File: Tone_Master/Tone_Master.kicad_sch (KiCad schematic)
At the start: 49 parts, among them J1 Barrel_Jack, J2 Barrel_Jack, Q1 2N3904, Q2 2N3904, SW2 DSP_EN, SW3 Chorus_EN, SW4 SW_Rotary_4x3, U1 TL072, U2 TL072

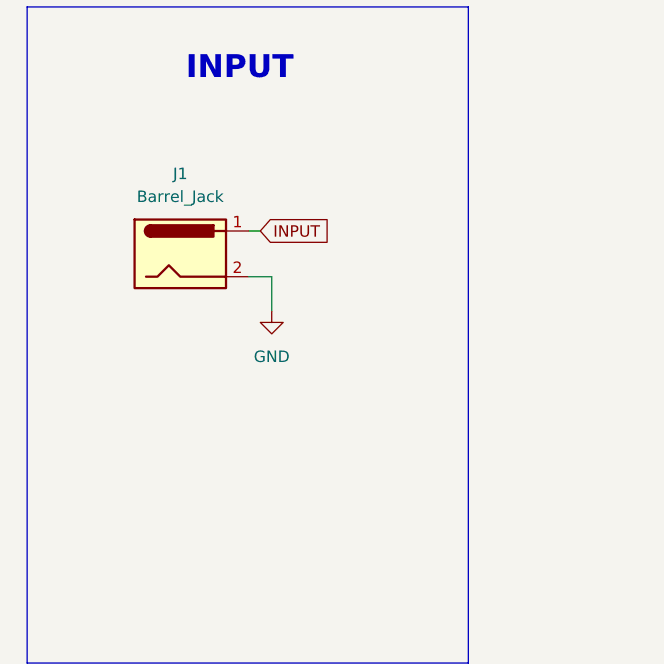
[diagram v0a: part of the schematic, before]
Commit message: add block diagram
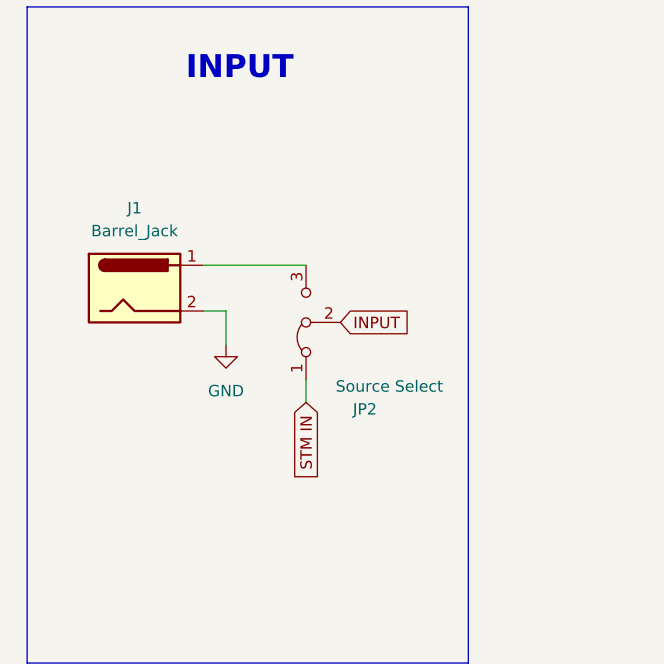
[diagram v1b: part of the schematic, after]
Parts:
- added JP2: Source Select, symbol Jumper:Jumper_3_Bridged12
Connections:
- net INPUT: now also JP2.2 (C); no longer J1.1
- new net: J1.1, JP2.3 (B)
- new net STM IN: JP2.1 (A)

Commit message: add BOM
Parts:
- removed C3: 50pF, Capacitor_THT:C_Rect_L7.2mm_W3.0mm_P5.00mm_FKS2_FKP2_MKS2_MKP2, symbol Device:C
- removed SW4: SW_Rotary_4x3, symbol Switch:SW_Rotary_4x3
- added C7: 50pF, Capacitor_THT:C_Rect_L7.2mm_W3.0mm_P5.00mm_FKS2_FKP2_MKS2_MKP2, symbol Device:C
- added R5, R6: 10K, Resistor_SMD:R_0805_2012Metric_Pad1.20x1.40mm_HandSolder, symbol Device:R
- added SW1: SW_Rotary_3x4, symbol Switch:SW_Rotary_3x4
- C5: renamed from C1; value 470nF -> 22nF
- renumbered C4 to C1, C13 to C10, C17 to C12, C15 to C13, C6 to C14, C12 to C15, C7 to C16, C5 to C17, C9 to C2, C2 to C3, C10 to C4, C18 to C6, C16 to C8, C8 to C9, D2 to D1, D1 to D2, J2 to J1, J1 to J2, JP2 to JP1, JP1 to JP2, Q2 to Q1, Q1 to Q2, R2 to R1, R13 to R10, R9 to R11, R7 to R12, R5 to R13, R8 to R14, R4 to R15, R14 to R16, R6 to R2, R1 to R4, R11 to R7, R12 to R8, R10 to R9, RV4 to RV2, RV2 to RV3, U2 to U1, U1 to U2
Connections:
- net DISTORT_IN: now also R6.2; no longer C5.1
- net DISTORT_OUT: now also SW1.10
- net FUZZ_OUT: now also SW1.11
- net GND: now also C7.2, SW1.7
- net OD_IN: now also R5.1; no longer C3.1
- net OD_OUT: now also SW1.9
- net Signal_OUT: now also SW1.15
- net at C4.1, D1.2 (A), D3.1 (K)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: now also SW1.1
- net at C9.2, RV1.2: now also SW1.13
- net at RV1.3: now also SW1.14
- net at U2.1: now also SW1.2
- net at C12.1: now also SW1.3
- net at C11.2: now also SW1.6
- net PICKUP_OUT: now reaches J2.1, JP1.3 (B)
- net STM IN renamed STM OUT
- new net: C3.1, R5.2
- new net: C5.1, C7.1, R6.1
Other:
- moved on the sheet: C5, R4, U1B

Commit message: Todo: input buffer
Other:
- note added: "PICKUP TO STM"
- moved on the sheet: U1B
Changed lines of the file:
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@@
 	(wire
 		(pts
-			(xy 45.72 210.82) (xy 59.69 210.82)
+			(xy 46.99 210.82) (xy 59.69 210.82)
 		)
 		(stroke
@@
 	)
 	(rectangle
-		(start 28.702 160.528)
-		(end 77.724 233.426)
+		(start 28.448 218.948)
+		(end 77.47 262.382)
+		(stroke
+			(width 0)
+			(type default)
+		)
+		(fill
+			(type none)
+		)
+	)
+	(rectangle
+		(start 28.702 173.228)
+		(end 77.724 216.916)
 		(stroke
 			(width 0)
@@
 	(text "INPUT"
 		(exclude_from_sim no)
-		(at 52.324 167.386 0)
+		(at 52.324 179.832 0)
 		(effects
 			(font
@@
 		(exclude_from_sim no)
 		(at 329.184 33.528 0)
+		(effects
+			(font
+				(size 2.54 2.54)
+				(thickness 0.254)
+				(bold yes)
+			)
+		)
+	)
+	(text "PICKUP TO STM"
+		(exclude_from_sim no)
+		(at 52.07 223.52 0)
 		(effects
 			(font
@@
 		)
 	)
-	(global_label "STM OUT"
+	(global_label "PICKUP_OUT"
 		(shape input)
-		(at 45.72 210.82 180)
+		(at 44.45 242.57 180)
 		(fields_autoplaced yes)
 		(effects
@@
 		)
 		(property "Intersheetrefs" "${INTERSHEET_REFS}"
-			(at 34.5101 210.82 0)
+			(at 29.8533 242.57 0)
 			(effects
 				(font
@@
 				)
 				(justify left)
+				(hide yes)
+			)
+		)
+	)
+	(global_label "STM OUT"
+		(shape input)
+		(at 46.99 210.82 180)
+		(fields_autoplaced yes)
+		(effects
+			(font
+				(size 1.27 1.27)
+			)
+			(justify right)
+		)
+		(property "Intersheetrefs" "${INTERSHEET_REFS}"
+			(at 35.7801 210.82 0)
+			(effects
+				(font
+					(size 1.27 1.27)
+				)
+				(justify right)
 				(hide yes)
 			)
@@
 	(symbol
 		(lib_id "Amplifier_Operational:TL072")
-		(at 441.96 187.96 0)
+		(at 57.15 245.11 0)
 		(unit 2)
 		(exclude_from_sim no)
@@
 		(dnp no)
 		(property "Reference" "U1"
-			(at 441.96 177.8 0)
+			(at 57.15 234.95 0)
 			(effects
 				(font
@@
 		)
 		(property "Value" "TL072"
-			(at 441.96 180.34 0)
+			(at 57.15 237.49 0)
 			(effects
 				(font
@@
 		)
 		(property "Footprint" "Package_DIP:DIP-8_W7.62mm"
-			(at 441.96 187.96 0)
+			(at 57.15 245.11 0)
 			(effects
 				(font
@@
 		)
 		(property "Datasheet" "http://www.ti.com/lit/ds/symlink/tl071.pdf"
-			(at 441.96 187.96 0)
+			(at 57.15 245.11 0)
 			(effects
 				(font
@@
 		)
 		(property "Description" "Dual Low-Noise JFET-Input Operational Amplifiers, DIP-8/SOIC-8"
-			(at 441.96 187.96 0)
-			(effects
-				(font
+			(at 57.15 245.11 0)
+			(effects
+				(font

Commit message: full schematic v1
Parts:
- removed J1: Barrel_Jack, Connector_BarrelJack:BarrelJack_SwitchcraftConxall_RAPC10U_Horizontal, symbol Connector:Barrel_Jack
- added C18, C19: 1uF, Capacitor_THT:CP_Radial_D8.0mm_P5.00mm, symbol Device:C_Polarized_Small_US
- added C20: 470nF, Capacitor_THT:C_Rect_L7.2mm_W3.0mm_P5.00mm_FKS2_FKP2_MKS2_MKP2, symbol Device:C
- added C21: 47uF, Capacitor_THT:CP_Radial_D8.0mm_P5.00mm, symbol Device:C_Polarized_Small_US
- added C22: 47nF, symbol Device:C
- added Q3: TIP41C, Package_TO_SOT_THT:TO-220-3_Vertical, symbol Transistor_BJT:TIP41C
- added Q4: TIP42C, Package_TO_SOT_THT:TO-220-3_Vertical, symbol Transistor_BJT:TIP42C
- added R19, R24: 1Meg, symbol Device:R
- added R22: 47k, symbol Device:R
- added R23: 3K, symbol Device:R
- added R25: 10k, symbol Device:R
- added R26: 22k, symbol Device:R
- added U3: TL072, Package_DIP:DIP-8_W7.62mm, symbol Amplifier_Operational:TL072
- added U4: ~, Black Pill:STM32 Black Pill, symbol STM32_Black_Pill:SW_DIP_x10
- added U5: LM7805_TO220, Package_TO_SOT_THT:TO-220-3_Horizontal_TabDown, symbol Regulator_Linear:LM7805_TO220
- added U6, U7: MCP4725xxx-xCH, Package_TO_SOT_SMD:SOT-23-6, symbol Analog_DAC:MCP4725xxx-xCH
- added U8: LP2950-3.3_TO92, Package_TO_SOT_THT:TO-92_Inline, symbol Regulator_Linear:LP2950-3.3_TO92
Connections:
- net +9V: now also Q3.2 (C), R22.1, U3.8 (V+), U5.1 (VI)
- net 4.5V_ref: now also C18.1, R19.1
- net GND: now also C21.2, C22.2, Q4.2 (C), R23.2, U3.4 (V-), U4.47 (GND), U5.2 (GND), U6.2 (VSS), U7.6 (GND), U8.2 (GND)
- net PICKUP_OUT: now also C20.1, U4.10 (A0)
- net STM OUT: now also U6.1 (VOUT)
- net at U1.5 (+): now also C20.2, R24.1
- net at U1.6 (-): now also R25.1, R26.1
- net Preamp_OUT: now reaches U1.7
- net Preamp_OUT: now also R26.2
- net OUTPUT: no longer names the net of RV3.2
- net OUTPUT: now also C18.2
- new net: C21.1, R22.2, R23.1, R24.2
- new net: C22.1, R25.2
- new net: Q3.1 (B), Q4.1 (B), U3.1
- new net: C19.1, Q3.3 (E), Q4.3 (E), U3.2 (-)
- new net: R19.2, U3.3 (+)
- new net: U7.5 (VDD), U8.1 (VO)
- new net 5V: U4.5V, U5.3 (VO), U6.3 (VDD), U8.3 (VI)
- new net AUDIO_OUT: C19.2
- new net SCK: U4.13 (A3), U7.3 (WS)
- new net SCL: U4.42 (B6), U6.5 (SCL)
- new net SD: U7.4 (SD)
- new net SDA: U4.43 (B7), U6.4 (SDA)
- new net WS: U4.12 (23), U7.3 (WS)
- no-connect marks 0 -> 30
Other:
- note added: "Black Pill"
- note added: "DAC"
- note added: "I^{2}S MIC MODULE"
- note added: "POWER AMPLIFIER"
- note removed: "OUTPUT"
- moved on the sheet: C1, C10, C11, C12, C13, C14, C15, C16, C17, C2, C3, C4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

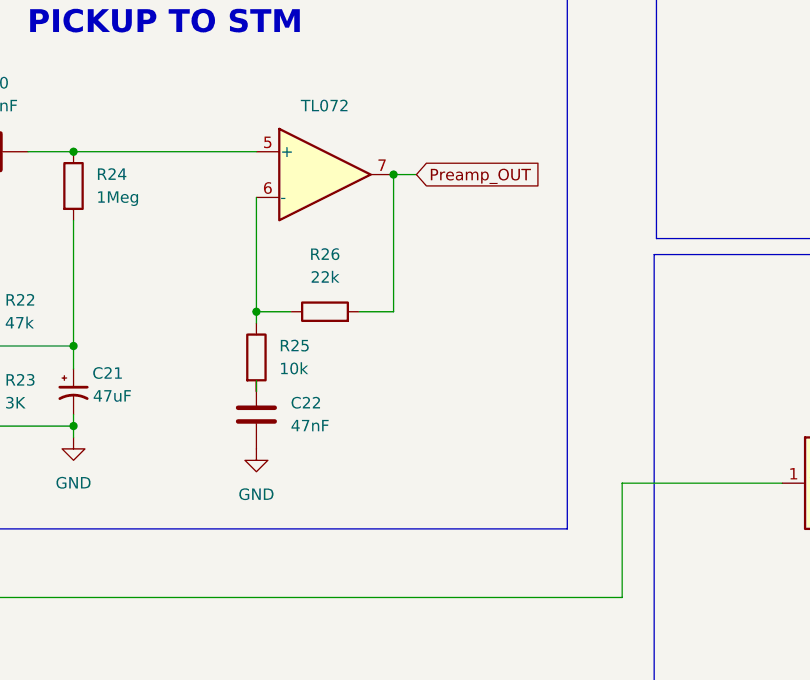
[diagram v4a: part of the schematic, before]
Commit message: Add voltage protection
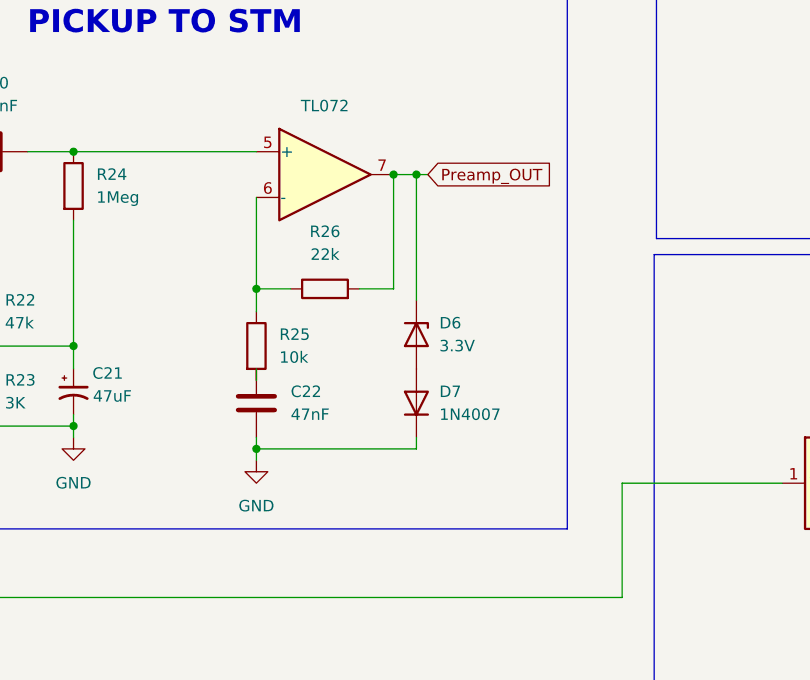
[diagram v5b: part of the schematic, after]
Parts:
- added D6: 3.3V, Diode_THT:D_DO-41_SOD81_P7.62mm_Horizontal, symbol Device:D_Zener
- added D7: 1N4007, Diode_THT:D_DO-41_SOD81_P7.62mm_Horizontal, symbol Device:D
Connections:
- net GND: now also D7.1 (K)
- net Preamp_OUT: now also D6.1 (K)
- new net: D6.2 (A), D7.2 (A)
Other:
- moved on the sheet: C22, R25, R26

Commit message: R2
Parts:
- removed D3: 1N4148, Diode_THT:D_DO-35_SOD27_P7.62mm_Horizontal, symbol Diode:1N4148
- removed JP2: Tone Control Select, symbol Jumper:Jumper_3_Bridged12
- removed Q3: TIP41C, Package_TO_SOT_THT:TO-220-3_Vertical, symbol Transistor_BJT:TIP41C
- removed Q4: TIP42C, Package_TO_SOT_THT:TO-220-3_Vertical, symbol Transistor_BJT:TIP42C
- removed R19: 1Meg, symbol Device:R
- removed unit 2 of U3
- removed unit 1 of U3
- removed U8: LP2950-3.3_TO92, Package_TO_SOT_THT:TO-92_Inline, symbol Regulator_Linear:LP2950-3.3_TO92
- added C23: 330n, Capacitor_THT:CP_Radial_D8.0mm_P5.00mm, symbol Device:C_Polarized_Small_US
- added C24: 10u, Capacitor_THT:C_Rect_L7.2mm_W3.0mm_P5.00mm_FKS2_FKP2_MKS2_MKP2, symbol Device:C
- added C25: 330n, Capacitor_THT:C_Rect_L7.2mm_W3.0mm_P5.00mm_FKS2_FKP2_MKS2_MKP2, symbol Device:C
- added C26: 47p, Capacitor_THT:C_Rect_L7.2mm_W3.0mm_P5.00mm_FKS2_FKP2_MKS2_MKP2, symbol Device:C
- added C27: 180n, Capacitor_THT:CP_Radial_D8.0mm_P5.00mm, symbol Device:C_Polarized_Small_US
- added R17: 10, Resistor_THT:R_Axial_DIN0309_L9.0mm_D3.2mm_P12.70mm_Horizontal, symbol Device:R
- added U8: LM386, symbol Amplifier_Audio:LM386
- C18: value 1uF -> 330n
- C19: value 1uF -> 1000uF
- C22: footprint (none) -> Capacitor_THT:C_Rect_L7.2mm_W3.0mm_P5.00mm_FKS2_FKP2_MKS2_MKP2
- D4: footprint LED_SMD:LED_1206_3216Metric_Pad1.42x1.75mm_HandSolder -> LED_THT:LED_D3.0mm_Clear
- D5: footprint (none) -> LED_THT:LED_D3.0mm_Clear
- JP1: footprint (none) -> Connector_PinHeader_2.54mm:PinHeader_1x02_P2.54mm_Vertical
- R1, R10, R11, R12, R13, R15, R16, R2, R3, R4, R5, R6, R7, R8: footprint Resistor_SMD:R_0805_2012Metric_Pad1.20x1.40mm_HandSolder -> Resistor_THT:R_Axial_DIN0309_L9.0mm_D3.2mm_P12.70mm_Horizontal
- R14: value 330K -> 680K; footprint Resistor_SMD:R_0805_2012Metric_Pad1.20x1.40mm_HandSolder -> Resistor_THT:R_Axial_DIN0309_L9.0mm_D3.2mm_P12.70mm_Horizontal
- R22, R24, R25: footprint (none) -> Resistor_THT:R_Axial_DIN0309_L9.0mm_D3.2mm_P12.70mm_Horizontal
- R23: value 3K -> 10K; footprint (none) -> Resistor_THT:R_Axial_DIN0309_L9.0mm_D3.2mm_P12.70mm_Horizontal
- R26: value 22k -> 33K; footprint (none) -> Resistor_THT:R_Axial_DIN0309_L9.0mm_D3.2mm_P12.70mm_Horizontal
- R9: value 10k -> 33K; footprint Resistor_SMD:R_0805_2012Metric_Pad1.20x1.40mm_HandSolder -> Resistor_THT:R_Axial_DIN0309_L9.0mm_D3.2mm_P12.70mm_Horizontal
- RV1: value 10K -> 100k
- SW2, SW3: footprint (none) -> Button_Switch_THT:SW_SPST_Omron_B3F-40xx
- U2: footprint (none) -> Package_DIP:DIP-8_W7.62mm
- U4: footprint Black Pill:STM32 Black Pill -> Module:Arduino_Nano
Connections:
- net Chorus is gone; now on net SW_Effect: SW3.2
- net DISTORT_OUT is gone; now on net DISTORT_IN: SW1.10
- net +9V: now also C25.1, U8.6 (V+)
- net 4.5V_ref: no longer C18.1
- net DSP: now also U4.15 (A5)
- net FUZZ_IN: now also SW1.11
- net FUZZ_OUT: no longer SW1.11
- net GND: now also C23.2, C24.2, C25.2, C26.1, C27.2, U8.4 (GND)
- net OD_IN: now also SW1.9
- net OD_OUT: no longer SW1.9
- net PICKUP_OUT: no longer U4.10 (A0)
- net Signal_OUT: now also C16.2, R16.2; no longer SW1.15
- net at C4.1, D1.2 (A), SW1.1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: now also D2.1 (K)
- net at C9.1, D1.1 (K), D2.2 (A)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: now also Q1.1 (E); no longer C8.1, Q2.2 (B)
- net SW_Effect: now reaches U4.16 (A6)
- net 3V3: now reaches U4.48 (3V3)
- net 3V3: now also U7.5 (VDD)
- net at C19.1: now also R17.1, U8.5
- net at R10.2: now also C8.1, Q2.2 (B); no longer Q1.1 (E)
- new net: C27.1, R17.2
- new net: C18.1, C26.2, U8.3 (+)
- new net: C23.1, U8.2 (-)
- new net: C24.1, U8.7 (BYPASS)
- new net PREAMP_OUT: U4.10 (A0)
- new net Signal_IN: SW1.15
- no-connect marks 30 -> 32
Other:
- note added: "GUITAR AMP, EFFECTS AND REALTIME TONE SAMPLER"
- moved on the sheet: C14, C19, D2, D6, D7, R10, R13, R24, RV1, U6

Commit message: Final
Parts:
- removed U6: MCP4725xxx-xCH, Package_TO_SOT_SMD:SOT-23-6, symbol Analog_DAC:MCP4725xxx-xCH
- added C28: 10u, Capacitor_THT:CP_Radial_D8.0mm_P5.00mm, symbol Device:C_Polarized_Small_US
- added C29: 330n, Capacitor_THT:CP_Radial_D8.0mm_P5.00mm, symbol Device:C_Polarized_Small_US
- added D3: 1N4148, Diode_THT:D_DO-35_SOD27_P7.62mm_Horizontal, symbol Diode:1N4148
- added R19: 22k, Resistor_THT:R_Axial_DIN0309_L9.0mm_D3.2mm_P12.70mm_Horizontal, symbol Device:R
- added R27, R30: 1Meg, Resistor_THT:R_Axial_DIN0309_L9.0mm_D3.2mm_P12.70mm_Horizontal, symbol Device:R
- added RV4: 10K, Potentiometer_THT:Potentiometer_Piher_PT-15-V02_Vertical, symbol Device:R_Potentiometer
- C13: value 47nF -> 100n
- C14: value 47nF -> 220n
- C18, C23: value 330n -> 270n
- C22: value 47nF -> 100pF
- C25: value 330n -> .33u
- C27: value 180n -> .1u
- C4: value 470nF -> 1uF
- C7: value 50pF -> 100pF
- C8: value 1uF -> 2.2uF
- C9: value 50pF -> 100p
- R10: value 100k -> 120k
- R11: value 680 -> 1k
- R12: value 4.7K -> 10k
- R23: value 10K -> 680
- R26: value 33K -> 120k
- RV3: value 500K -> 470K
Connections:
- net FUZZ_OUT is gone; now on net STM_OUT: C6.2
- net OD_OUT is gone; now on net STM_OUT: C4.2
- net STM OUT is gone; now on an unnamed net: JP1.1 (A)
- net Signal_IN is gone; now on net PICKUP_OUT: SW1.15
- net Signal_OUT is gone; now on net STM_OUT: C16.2, R16.2
- net DISTORT_IN: no longer SW1.10
- net GND: now also R25.2, R27.2, R30.2
- net OD_IN: no longer SW1.9
- net PICKUP_OUT: no longer C20.1
- net Preamp_OUT: now also C20.1, C22.1, R30.1
- net at C4.1, D1.2 (A), U1.1: now also D3.1 (K), R19.2; no longer D2.1 (K), SW1.1
- net Preamp_IN: now reaches SW1.12
- net Preamp_IN: now also SW1.10, SW1.9
- net at U8.1 (GAIN): now also C28.1
- net at U8.8 (GAIN): now also RV4.3
- net Distortion_OUT renamed STM_OUT
- net STM_OUT: now also C29.1, R27.1
- net INPUT: no longer names the net of JP1.2 (C)
- net INPUT: now also C29.2
- net SCL: no longer names the net of U4.42 (B6)
- net SDA: no longer names the net of U4.43 (B7)
- new net: D2.1 (K), D3.2 (A)
- new net: R19.1, SW1.1
- new net: C28.2, RV4.2
- no-connect marks 32 -> 35
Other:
- note added: "PREAMP"
- note added: "Trimpot"
- note removed: "DAC"
- note removed: "PICKUP TO STM"
- moved on the sheet: C19, C20, C27, D2, R17

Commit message: V1.0
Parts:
- removed C22: 100pF, Capacitor_THT:C_Rect_L7.2mm_W3.0mm_P5.00mm_FKS2_FKP2_MKS2_MKP2, symbol Device:C
- removed C29: 330n, Capacitor_THT:CP_Radial_D8.0mm_P5.00mm, symbol Device:C_Polarized_Small_US
- removed D6: 3.3V, Diode_THT:D_DO-41_SOD81_P7.62mm_Horizontal, symbol Device:D_Zener
- removed D7: 1N4007, Diode_THT:D_DO-41_SOD81_P7.62mm_Horizontal, symbol Device:D
- removed JP1: Source Select, Connector_PinHeader_2.54mm:PinHeader_1x02_P2.54mm_Vertical, symbol Jumper:Jumper_3_Bridged12
- removed R30: 1Meg, Resistor_THT:R_Axial_DIN0309_L9.0mm_D3.2mm_P12.70mm_Horizontal, symbol Device:R
- removed SW2: DSP_EN, Button_Switch_THT:SW_SPST_Omron_B3F-40xx, symbol Switch:SW_Push
- removed SW3: Chorus_EN, Button_Switch_THT:SW_SPST_Omron_B3F-40xx, symbol Switch:SW_Push
- removed U4: ~, Module:Arduino_Nano, symbol STM32_Black_Pill:SW_DIP_x10
- removed U5: LM7805_TO220, Package_TO_SOT_THT:TO-220-3_Horizontal_TabDown, symbol Regulator_Linear:LM7805_TO220
- removed U7: MCP4725xxx-xCH, Package_TO_SOT_SMD:SOT-23-6, symbol Analog_DAC:MCP4725xxx-xCH
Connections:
- net DISTORT_IN is gone; now on net Preamp_OUT: R6.2
- net OD_IN is gone; now on net Preamp_OUT: R5.1
- net Preamp_IN: now also C20.1
- net Preamp_OUT: no longer C20.1
- net STM_OUT renamed DISTORT_OUT
- no-connect marks 35 -> 4
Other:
- note removed: "Black Pill"
- note removed: "DSP/SOFTWARE FX EN"
- note removed: "I^{2}S MIC MODULE"
- moved on the sheet: C16, C17, J2, R15, R16, R27, RV2, RV3
